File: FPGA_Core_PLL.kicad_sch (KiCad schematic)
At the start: 6 parts, among them U1 NX1H35 PBGA625, U4 AS4C8M16SA-6BIN

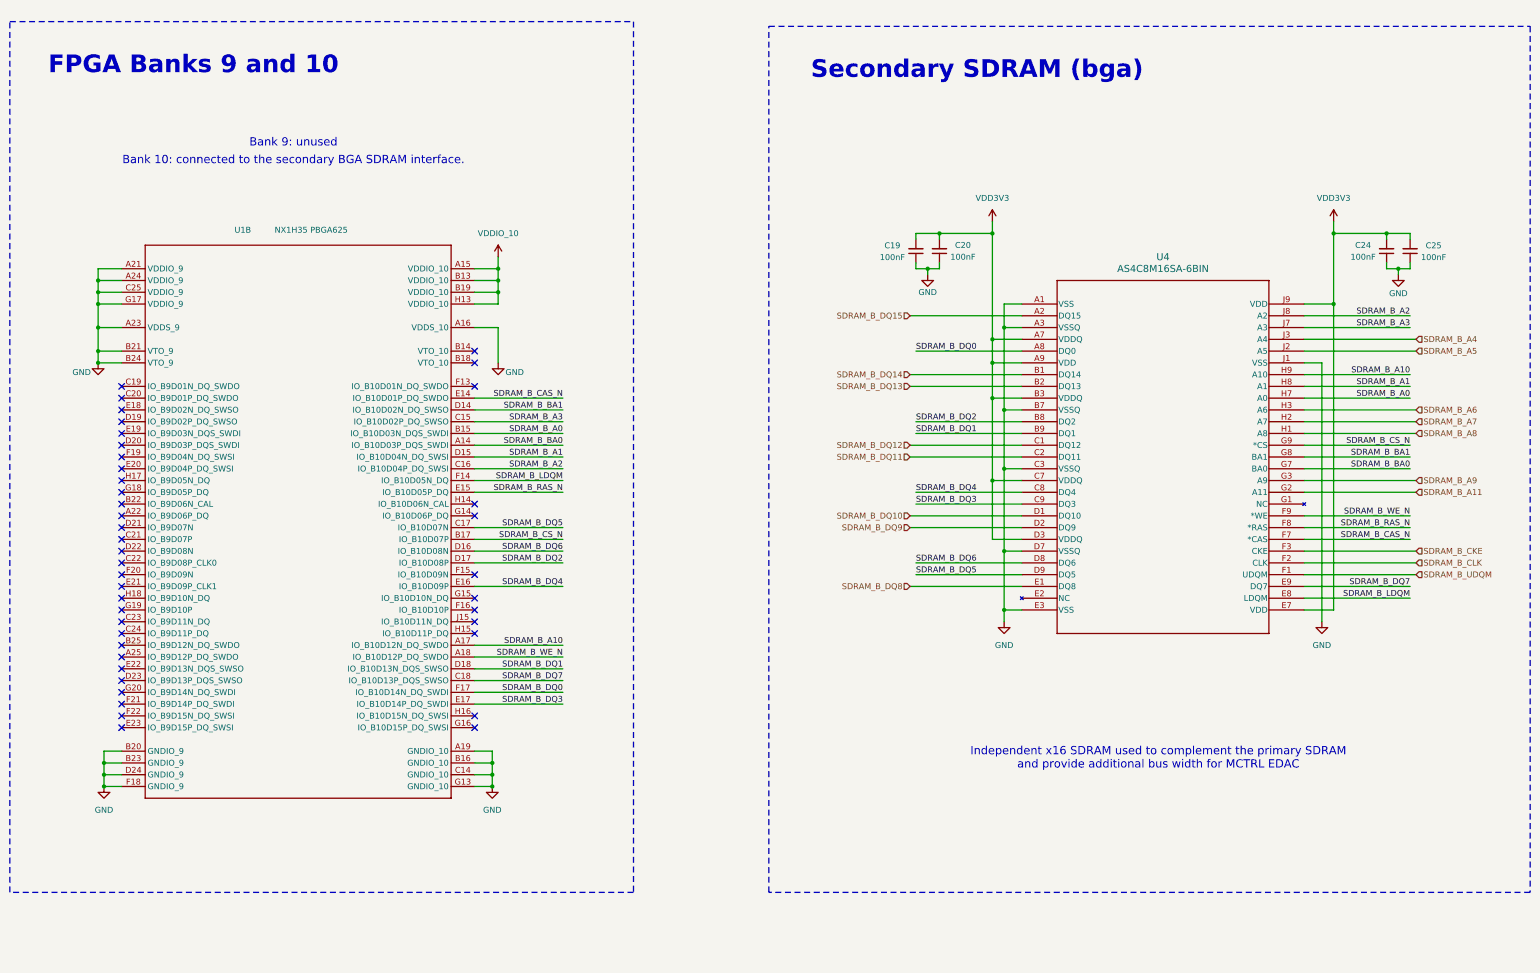
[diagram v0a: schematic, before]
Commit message: pre order checks
ADDED jumper for VDDSENSE remote sensing / 1V2 core PWR for MAX LDO feedback
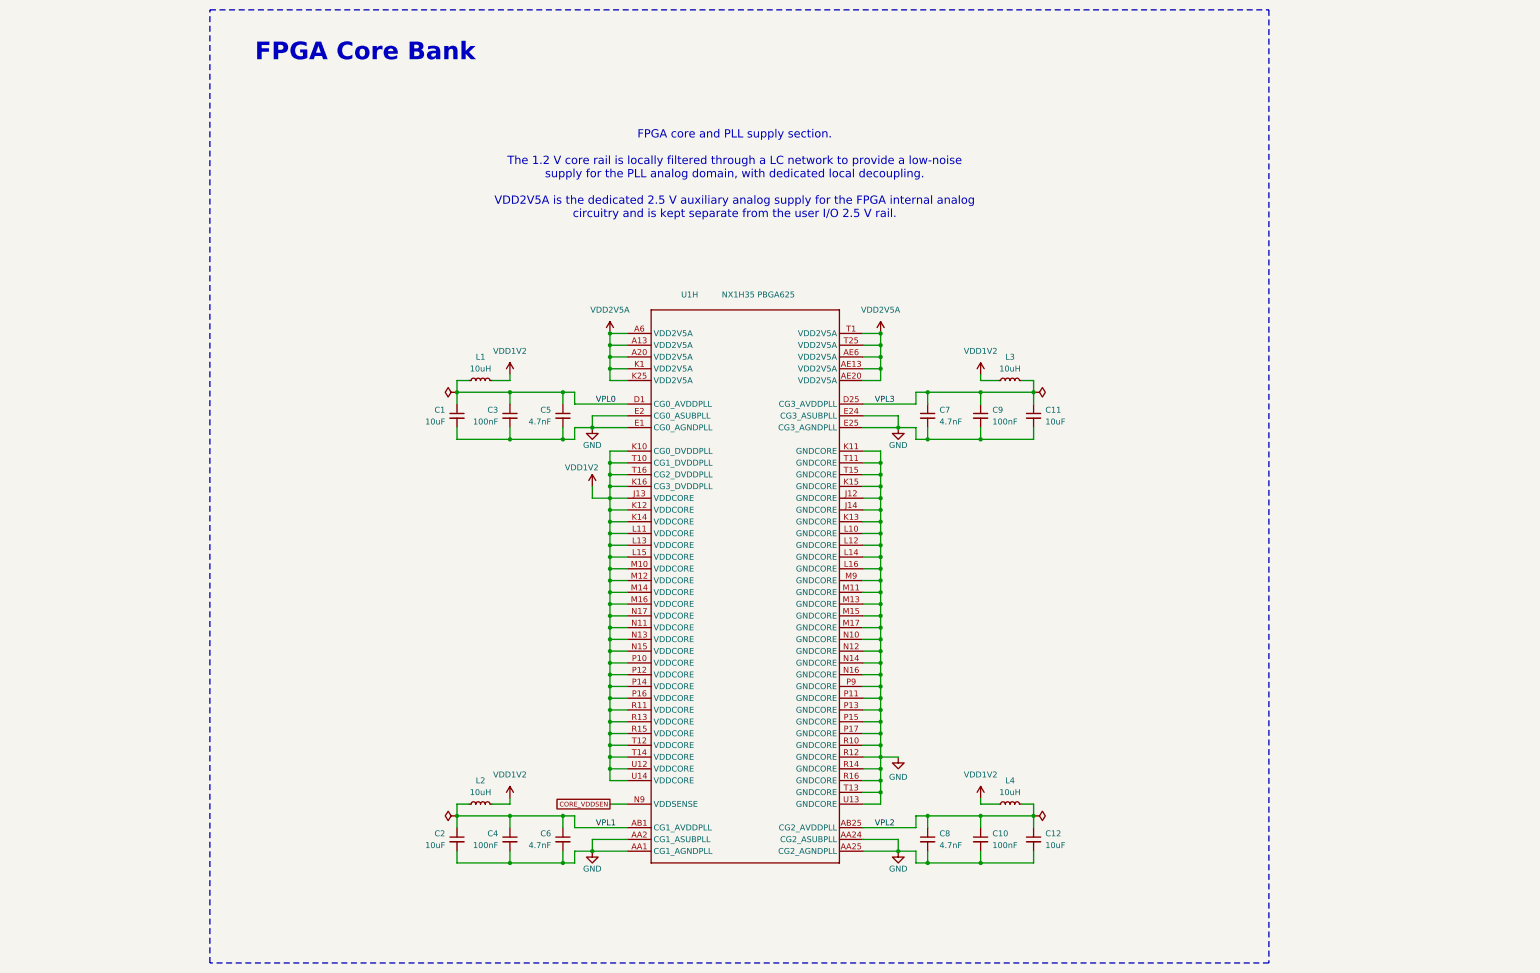
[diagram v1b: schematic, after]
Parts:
- removed C19, C20, C24, C25: 100nF, Capacitor_SMD:C_0402_1005Metric_Pad0.74x0.62mm_HandSolder, symbol Device:C_Small
- removed U1: NX1H35 PBGA625, DataHub_NG_Medium:NX1H35S_CLGA625, symbol Brave625:root_0_BRAVE625A_Brave625.SchLib
- removed U4: AS4C8M16SA-6BIN, DataHub_Footprints:sdram2_bga_TFBGA-54_8X8_ALL, symbol SDRAM_BGA_8x16:AS4C8M16S-6BIN
- added C1, C11, C12, C2: 10uF, Capacitor_SMD:C_0603_1608Metric_Pad1.08x0.95mm_HandSolder, symbol Device:C_Small
- added C10, C3, C4, C9: 100nF, Capacitor_SMD:C_0402_1005Metric_Pad0.74x0.62mm_HandSolder, symbol Device:C_Small
- added C5, C6, C7, C8: 4.7nF, Capacitor_SMD:C_0402_1005Metric_Pad0.74x0.62mm_HandSolder, symbol Device:C_Small
- added L1, L2, L3, L4: 10uH, Inductor_SMD:L_0603_1608Metric_Pad1.05x0.95mm_HandSolder, symbol Device:L_Small
- added U1: NX1H35 PBGA625, DataHub_NG_Medium:NX1H35S_CLGA625, symbol Brave625:root_0_BRAVE625A_Brave625.SchLib
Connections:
- net GND: now also C1.2, C10.2, C11.2, C12.2, C2.2, C3.2, C4.2, C5.2, C6.2, C7.2, C8.2, C9.2, U1.AA1 (CG1_AGNDPLL), U1.AA2 (CG1_ASUBPLL), U1.AA24 (CG2_ASUBPLL), U1.AA25 (CG2_AGNDPLL), U1.E1 (CG0_AGNDPLL), U1.E2 (CG0_ASUBPLL), U1.E24 (CG3_ASUBPLL), U1.E25 (CG3_AGNDPLL), U1.J12 (GNDCORE), U1.J14 (GNDCORE), U1.K11 (GNDCORE), U1.K13 (GNDCORE), U1.K15 (GNDCORE), U1.L10 (GNDCORE), U1.L12 (GNDCORE), U1.L14 (GNDCORE), U1.L16 (GNDCORE), U1.M11 (GNDCORE), U1.M13 (GNDCORE), U1.M15 (GNDCORE), U1.M17 (GNDCORE), U1.M9 (GNDCORE), U1.N10 (GNDCORE), U1.N12 (GNDCORE), U1.N14 (GNDCORE), U1.N16 (GNDCORE), U1.P11 (GNDCORE), U1.P13 (GNDCORE), U1.P15 (GNDCORE), U1.P17 (GNDCORE), U1.P9 (GNDCORE), U1.R10 (GNDCORE), U1.R12 (GNDCORE), U1.R14 (GNDCORE), U1.R16 (GNDCORE), U1.T11 (GNDCORE), U1.T13 (GNDCORE), U1.T15 (GNDCORE), U1.U13 (GNDCORE)
- new net CORE_VDDSEN: U1.N9 (VDDSENSE)
- new net VDD1V2: L1.1, L2.1, L3.1, L4.1, U1.J13 (VDDCORE), U1.K10 (CG0_DVDDPLL), U1.K12 (VDDCORE), U1.K14 (VDDCORE), U1.K16 (CG3_DVDDPLL), U1.L11 (VDDCORE), U1.L13 (VDDCORE), U1.L15 (VDDCORE), U1.M10 (VDDCORE), U1.M12 (VDDCORE), U1.M14 (VDDCORE), U1.M16 (VDDCORE), U1.N11 (VDDCORE), U1.N13 (VDDCORE), U1.N15 (VDDCORE), U1.N17 (VDDCORE), U1.P10 (VDDCORE), U1.P12 (VDDCORE), U1.P14 (VDDCORE), U1.P16 (VDDCORE), U1.R11 (VDDCORE), U1.R13 (VDDCORE), U1.R15 (VDDCORE), U1.T10 (CG1_DVDDPLL), U1.T12 (VDDCORE), U1.T14 (VDDCORE), U1.T16 (CG2_DVDDPLL), U1.U12 (VDDCORE), U1.U14 (VDDCORE)
- new net VDD2V5A: U1.A13 (VDD2V5A), U1.A20 (VDD2V5A), U1.A6 (VDD2V5A), U1.AE13 (VDD2V5A), U1.AE20 (VDD2V5A), U1.AE6 (VDD2V5A), U1.K1 (VDD2V5A), U1.K25 (VDD2V5A), U1.T1 (VDD2V5A), U1.T25 (VDD2V5A)
- new net VPL0: C1.1, C3.1, C5.1, L1.2, U1.D1 (CG0_AVDDPLL)
- new net VPL1: C2.1, C4.1, C6.1, L2.2, U1.AB1 (CG1_AVDDPLL)
- new net VPL2: C10.1, C12.1, C8.1, L4.2, U1.AB25 (CG2_AVDDPLL)
- new net VPL3: C11.1, C7.1, C9.1, L3.2, U1.D25 (CG3_AVDDPLL)
- no-connect marks 42 -> 0
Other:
- note added: "FPGA Core Bank"
- note added: "FPGA core and PLL supply section. The 1.2 V core rail is locally filtered through a LC network to provide a low-noise supply for the PLL analog domain, with dedicated local decoupling. VDD2V5A is the dedicated 2.5 V auxiliary analog supply for the FPGA internal analog circuitry and is kept separate from the user I/O 2.5 V rail."
- note removed: "Bank 10: connected to the secondary BGA SDRAM interface."
- note removed: "Bank 9: unused"
- note removed: "FPGA Banks 9 and 10"
- note removed: "Independent x16 SDRAM used to complement the primary SDRAM and provide additional bus width for MCTRL EDAC"
- note removed: "Secondary SDRAM (bga)"
- company: (none) -> KTH Royal Institute of Technology
- title: (none) -> FPGA Core and PLL Supplies
